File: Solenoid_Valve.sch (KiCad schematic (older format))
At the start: 62 parts, among them IC1 Si8621AB-B-ISR, J1 Bus_mechaken_PCIexpress_x16_1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, J10 Conn_01x02, J11 Conn_01x02, J12 Conn_01x02, J13 Conn_01x02, J14 Conn_01x02, J15 Conn_01x02, J16 Conn_01x02, J17 Conn_01x02, J18 Conn_01x02, J19 Conn_01x02, J2 Conn_01x05, J20 Conn_01x02, J3 Conn_01x02, J4 Conn_01x02, J5 Conn_01x02, J6 Conn_01x02, J7 Conn_01x03, J8 Conn_01x02, J9 Conn_01x02, Q1 ULN2004D1013TR, Q2 ULN2004D1013TR, Q3 ULN2004D1013TR, SW1 SW_Push, U1 LDL1117S33R, U2 STM32F042K6Tx, U3 MCP2562-E-SN, U4 L7812, U5 LDL1117S33R

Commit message: change
Remove NRST SW
clean
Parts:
- removed C3: 0.1uF, Capacitor_SMD:C_0805_2012Metric, symbol Device:C
- removed R3: 10K, Resistor_SMD:R_0603_1608Metric, symbol Device:R
- removed SW1: SW_Push, SamacSys_Parts:PTS647SM38SMTR2LFS, symbol Switch:SW_Push
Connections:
- wire segments 137 -> 131
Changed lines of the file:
@@
 EESchema Schematic File Version 4
-LIBS:Solenoid_Valve-cache
 EELAYER 30 0
 EELAYER END
@@
 Connection ~ 1350 1950
 Wire Wire Line
-	2800 1150 2800 1300
-Wire Wire Line
-	3700 1150 2800 1150
-Wire Wire Line
 	5450 3000 5450 3100
 Wire Wire Line
@@
 Wire Wire Line
 	900  1650 1000 1650
-Wire Wire Line
-	2300 2000 2800 2000
-Wire Wire Line
-	2300 1600 2800 1600
 Wire Wire Line
 	3700 1150 3950 1150
@@
 	3700 1050 3700 1150
 Connection ~ 3700 1150
-Connection ~ 2800 1600
 Wire Wire Line
 	3700 3300 3700 3400
@@
 Text GLabel 5750 3400 0    50   Input ~ 0
 NRST
-Text GLabel 3100 1600 1    50   Input ~ 0
+Text GLabel 3200 1600 0    50   Input ~ 0
 NRST
 Text GLabel 4200 3100 2    50   Input ~ 0
@@
 $EndComp
 $Comp
-L Switch:SW_Push SW1
-U 1 1 5D5B7C98
-P 2800 1800
-F 0 "SW1" V 2754 1752 50  0000 R CNN
-F 1 "SW_Push" V 2845 1752 50  0000 R CNN
-F 2 "SamacSys_Parts:PTS647SM38SMTR2LFS" H 2800 2000 50  0001 C CNN
-F 3 "~" H 2800 2000 50  0001 C CNN
-	1    2800 1800
-	0    -1   1    0
-$EndComp
-$Comp
-L Device:C C3
-U 1 1 5D5B9AC3
-P 2300 1750
-F 0 "C3" H 2415 1796 50  0000 L CNN
-F 1 "0.1uF" H 2415 1705 50  0000 L CNN
-F 2 "Capacitor_SMD:C_0805_2012Metric" H 2338 1600 50  0001 C CNN
-F 3 "~" H 2300 1750 50  0001 C CNN
-	1    2300 1750
-	1    0    0    -1
-$EndComp
-$Comp
-L Device:R R3
-U 1 1 5D5C9315
-P 2800 1450
-F 0 "R3" H 2870 1496 50  0000 L CNN
-F 1 "10K" H 2870 1405 50  0000 L CNN
-F 2 "Resistor_SMD:R_0603_1608Metric" V 2730 1450 50  0001 C CNN
-F 3 "~" H 2800 1450 50  0001 C CNN
-	1    2800 1450
-	1    0    0    -1
-$EndComp
-$Comp
 L Device:R R2
 U 1 1 5D5AB267
@@
 	0    1    1    0
 $EndComp
-Wire Wire Line
-	2300 1900 2300 2000
 Text Label 2850 3100 0    50   ~ 0
 BOOT
@@
 Wire Wire Line
 	6100 1350 6100 1450
-Text GLabel 5300 1150 0    50   Output ~ 0
+Text GLabel 5300 1350 0    50   Output ~ 0
 DIP_SW_1
-Text GLabel 5300 1250 0    50   Output ~ 0
+Text GLabel 5300 1450 0    50   Output ~ 0
 DIP_SW_2
-Wire Wire Line
-	3200 1600 2800 1600
 Connection ~ 3700 3300
 Wire Wire Line
@@
 	0    -1   -1   0
 $EndComp
-$Comp
-L power:GNDPWR #PWR05
-U 1 1 5DDA84FA
-P 2300 2000
-F 0 "#PWR05" H 2300 1800 50  0001 C CNN
-F 1 "GNDPWR" H 2300 1870 50  0000 C CNN
-F 2 "" H 2300 1950 50  0001 C CNN
-F 3 "" H 2300 1950 50  0001 C CNN
-	1    2300 2000
-	1    0    0    -1
-$EndComp
-Connection ~ 2300 2000
 $Comp
 L power:+3.3V #PWR01
@@
 Text GLabel 4200 2400 2    50   Input ~ 0
 IC_C3
-NoConn ~ 5300 1350
-NoConn ~ 5300 1450
 $Comp
 L power:GNDPWR #PWR0120
@@
 NoConn ~ 1150 7000
 $Comp
-L power:GNDPWR #PWR?
+L power:GNDPWR #PWR0115
 U 1 1 5DF51C19
 P 5250 1900
-F 0 "#PWR?" H 5250 1700 50  0001 C CNN
+F 0 "#PWR0115" H 5250 1700 50  0001 C CNN
 F 1 "GNDPWR" H 5250 1770 50  0000 C CNN
 F 2 "" H 5250 1850 50  0001 C CNN
@@
 	0    1    1    0
 $EndComp
+NoConn ~ 5300 1150
+NoConn ~ 5300 1250
 $EndSCHEMATC

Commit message: Prototype-1.1
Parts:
- Q1, Q2, Q3: symbol dk_Transistors-Bipolar-BJT-Arrays:ULN2003D1013TR -> Solenoid_Valve-rescue:ULN2003D1013TR-dk_Transistors-Bipolar-BJT-Arrays
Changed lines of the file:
@@
 DIP_SW_2
 $Comp
-L dk_Transistors-Bipolar-BJT-Arrays:ULN2003D1013TR Q1
+L Solenoid_Valve-rescue:ULN2003D1013TR-dk_Transistors-Bipolar-BJT-Arrays Q1
 U 1 1 5DC2DB55
 P 7500 2150
@@
 $EndComp
 $Comp
-L dk_Transistors-Bipolar-BJT-Arrays:ULN2003D1013TR Q2
+L Solenoid_Valve-rescue:ULN2003D1013TR-dk_Transistors-Bipolar-BJT-Arrays Q2
 U 1 1 5DC99CAB
 P 7500 3550
@@
 $EndComp
 $Comp
-L dk_Transistors-Bipolar-BJT-Arrays:ULN2003D1013TR Q3
+L Solenoid_Valve-rescue:ULN2003D1013TR-dk_Transistors-Bipolar-BJT-Arrays Q3
 U 1 1 5DCA1834
 P 7500 4950

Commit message: fix
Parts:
- C7: value 1uF -> 0.33uF
- C8: value 4.7uF -> 0.1uF
- J1: footprint PCIe:BUS_mechaken_PCIexpress_x16_164_Position -> PCIe:BUS_mechaken_PCIexpress_x16
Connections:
- net +3V3: no longer R2.2
- net GNDPWR: now also R2.2
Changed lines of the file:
@@
 	1    0    0    -1
-$EndComp
-$Comp
-L power:+3V3 #PWR08
-U 1 1 5DE307DF
-P 2500 3100
-F 0 "#PWR08" H 2500 2950 50  0001 C CNN
-F 1 "+3V3" H 2500 3240 50  0000 C CNN
-F 2 "" H 2500 3100 50  0001 C CNN
-F 3 "" H 2500 3100 50  0001 C CNN
-	1    2500 3100
-	-1   0    0    1
 $EndComp
 Text GLabel 3200 2500 0    50   Input ~ 0
@@
 P 7250 1150
 F 0 "C8" H 7275 1250 50  0000 L CNN
-F 1 "4.7uF" H 7275 1050 50  0000 L CNN
+F 1 "0.1uF" H 7275 1050 50  0000 L CNN
 F 2 "Capacitor_SMD:C_0805_2012Metric" H 7288 1000 50  0001 C CNN
 F 3 "~" H 7250 1150 50  0001 C CNN
@@
 P 6650 1150
 F 0 "C7" H 6675 1250 50  0000 L CNN
-F 1 "1uF" H 6675 1050 50  0000 L CNN
+F 1 "0.33uF" H 6675 1050 50  0000 L CNN
 F 2 "Capacitor_SMD:C_0805_2012Metric_Pad1.15x1.40mm_HandSolder" H 6688 1000 50  0001 C CNN
 F 3 "~" H 6650 1150 50  0001 C CNN
@@
 F 0 "J1" H 1700 12100 50  0000 C CNN
 F 1 "Bus_mechaken_PCIexpress_x16_164_Position" H 1650 10700 50  0000 C CNN
-F 2 "PCIe:BUS_mechaken_PCIexpress_x16_164_Position" H 1350 8900 50  0001 C CNN
+F 2 "PCIe:BUS_mechaken_PCIexpress_x16" H 1350 8900 50  0001 C CNN
 F 3 "http://pinouts.ru/Slots/PCI_pinout.shtml" H 1350 8900 50  0001 C CNN
 	1    1700 9000
@@
 NoConn ~ 5300 1150
 NoConn ~ 5300 1250
+$Comp
+L power:GNDPWR #PWR?
+U 1 1 5E334F41
+P 2500 3100
+F 0 "#PWR?" H 2500 2900 50  0001 C CNN
+F 1 "GNDPWR" H 2500 2970 50  0000 C CNN
+F 2 "" H 2500 3050 50  0001 C CNN
+F 3 "" H 2500 3050 50  0001 C CNN
+	1    2500 3100
+	1    0    0    -1
+$EndComp
 $EndSCHEMATC

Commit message: Release
Prototype-1.3をリリース
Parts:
- removed D1: LED, Diode_SMD:D_0603_1608Metric, symbol Device:LED
- removed R1: 10K, Resistor_SMD:R_0603_1608Metric, symbol Device:R
- added D11: D_Schottky, Diode_SMD:D_0603_1608Metric_Pad1.05x0.95mm_HandSolder, symbol Device:D_Schottky
- C1: renamed from C4; value 0.1uF -> 0.1u; footprint Capacitor_SMD:C_0805_2012Metric -> Capacitor_SMD:C_0805_2012Metric_Pad1.15x1.40mm_HandSolder
- C2: renamed from C7; value 0.33uF -> 0.33u
- C3: renamed from C8; value 0.1uF -> 0.1u; footprint Capacitor_SMD:C_0805_2012Metric -> Capacitor_SMD:C_0805_2012Metric_Pad1.15x1.40mm_HandSolder
- C4: renamed from C1; value 1.0uF -> 1.0u; footprint Capacitor_SMD:C_0805_2012Metric -> Capacitor_SMD:C_0805_2012Metric_Pad1.15x1.40mm_HandSolder
- C5: renamed from C2; value 4.7uF -> 2.2u; footprint Capacitor_SMD:C_0805_2012Metric -> Capacitor_SMD:C_0805_2012Metric_Pad1.15x1.40mm_HandSolder
- C6: value 0.1uF -> 0.1u; footprint Capacitor_SMD:C_0805_2012Metric -> Capacitor_SMD:C_0805_2012Metric_Pad1.15x1.40mm_HandSolder
- C7: renamed from C9; value 1.0uF -> 1.0u; footprint Capacitor_SMD:C_0805_2012Metric -> Capacitor_SMD:C_0805_2012Metric_Pad1.15x1.40mm_HandSolder
- C8: renamed from C10; value 4.7uF -> 4.7u; footprint Capacitor_SMD:C_0805_2012Metric -> Capacitor_SMD:C_0805_2012Metric_Pad1.15x1.40mm_HandSolder
- C9: renamed from C5; value 0.1uF -> 0.1u; footprint Capacitor_SMD:C_0805_2012Metric -> Capacitor_SMD:C_0805_2012Metric_Pad1.15x1.40mm_HandSolder
- D1: renamed from D6; footprint Diode_SMD:D_2010_5025Metric -> Diode_SMD:D_2010_5025Metric_Pad1.52x2.65mm_HandSolder
- D10: renamed from D17; footprint Diode_SMD:D_2010_5025Metric -> Diode_SMD:D_2010_5025Metric_Pad1.52x2.65mm_HandSolder
- D12: footprint Diode_SMD:D_2010_5025Metric -> Diode_SMD:D_2010_5025Metric_Pad1.52x2.65mm_HandSolder
- D13: renamed from D18; footprint Diode_SMD:D_2010_5025Metric -> Diode_SMD:D_2010_5025Metric_Pad1.52x2.65mm_HandSolder
- D14: renamed from D2; footprint Diode_SMD:D_2010_5025Metric -> Diode_SMD:D_2010_5025Metric_Pad1.52x2.65mm_HandSolder
- D15: renamed from D16; footprint Diode_SMD:D_2010_5025Metric -> Diode_SMD:D_2010_5025Metric_Pad1.52x2.65mm_HandSolder
- D16: renamed from D3; footprint Diode_SMD:D_2010_5025Metric -> Diode_SMD:D_2010_5025Metric_Pad1.52x2.65mm_HandSolder
- D17: renamed from D10; footprint Diode_SMD:D_2010_5025Metric -> Diode_SMD:D_2010_5025Metric_Pad1.52x2.65mm_HandSolder
- D18: renamed from D4; footprint Diode_SMD:D_2010_5025Metric -> Diode_SMD:D_2010_5025Metric_Pad1.52x2.65mm_HandSolder
- D2: renamed from D9; footprint Diode_SMD:D_2010_5025Metric -> Diode_SMD:D_2010_5025Metric_Pad1.52x2.65mm_HandSolder
- D3: renamed from D7; footprint Diode_SMD:D_2010_5025Metric -> Diode_SMD:D_2010_5025Metric_Pad1.52x2.65mm_HandSolder
- D4: renamed from D14; footprint Diode_SMD:D_2010_5025Metric -> Diode_SMD:D_2010_5025Metric_Pad1.52x2.65mm_HandSolder
- D5: renamed from D8; footprint Diode_SMD:D_2010_5025Metric -> Diode_SMD:D_2010_5025Metric_Pad1.52x2.65mm_HandSolder
- D6: renamed from D15; footprint Diode_SMD:D_2010_5025Metric -> Diode_SMD:D_2010_5025Metric_Pad1.52x2.65mm_HandSolder
- D7: renamed from D19; footprint Diode_SMD:D_2010_5025Metric -> Diode_SMD:D_2010_5025Metric_Pad1.52x2.65mm_HandSolder
- D8: renamed from D13; footprint Diode_SMD:D_2010_5025Metric -> Diode_SMD:D_2010_5025Metric_Pad1.52x2.65mm_HandSolder
- D9: renamed from D11; footprint Diode_SMD:D_2010_5025Metric -> Diode_SMD:D_2010_5025Metric_Pad1.52x2.65mm_HandSolder
- J10: renamed from J2; footprint Connector_JST:JST_XH_B5B-XH-A_1x05_P2.50mm_Vertical -> Connector_PinHeader_2.54mm:PinHeader_1x05_P2.54mm_Vertical
- J5: renamed from J7; footprint Connector_JST:JST_XH_B3B-XH-A_1x03_P2.50mm_Vertical -> Connector_PinHeader_2.54mm:PinHeader_1x03_P2.54mm_Vertical
- R1: renamed from R2; footprint Resistor_SMD:R_0603_1608Metric -> Resistor_SMD:R_0603_1608Metric_Pad1.05x0.95mm_HandSolder
- S1: footprint SamacSys_Parts:SOP254P980X370-8N -> Package_DIP:DIP-8_W7.62mm; symbol SamacSys_Parts:IKD0403101 -> Switch:SW_DIP_x04; Description 4 Way Surface Mount DIP Switch SPST, Raised Actuator Slide 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 -> (none); Height 3.7 -> (none); Manufacturer_Name Apem -> (none); Manufacturer_Part_Number IKD0403101 -> (none); RS Part Number 8772264 -> (none); RS Price/Stock http://uk.rs-online.com/web/p/products/8772264 -> (none)
- U1: renamed from U4; value L7812 -> NJM7812
- U2: renamed from U1; value LDL1117S33R -> AP2210N-3.3TRG1; footprint Package_TO_SOT_SMD:SOT-223-3_TabPin2 -> Package_TO_SOT_SMD:SOT-23_Handsoldering; symbol Solenoid_Valve-rescue:AP1117-33-Regulator_Linear -> Regulator_Linear:LD1117S33TR_SOT223
- U4: renamed from U5; value LDL1117S33R -> AP2210N-3.3TRG1; footprint Package_TO_SOT_SMD:SOT-223-3_TabPin2 -> Package_TO_SOT_SMD:SOT-23_Handsoldering; symbol Solenoid_Valve-rescue:AP1117-33-Regulator_Linear -> Regulator_Linear:LD1117S33TR_SOT223
- renumbered J8 to J1, J12 to J11, J18 to J12, J19 to J14, J4 to J15, J17 to J16, J5 to J17, J11 to J18, J6 to J19, J10 to J2, J1 to J20, J15 to J4, J9 to J6, J16 to J7, J20 to J8, J14 to J9, U2 to U3, U3 to U5
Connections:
- net 3.3V: now also S1.1, S1.2, D11.2 (A); no longer S1.5, S1.6, S1.7, S1.8
- net DIP_SW_1: now also S1.8, U3.28 (PB5); no longer S1.3, U3.29 (PB6)
- net DIP_SW_2: now also S1.7, U3.29 (PB6); no longer S1.4, U3.30 (PB7)
- net IC_A1: now also Q1.7 (IN_7), U3.30 (PB7); no longer Q1.1 (IN_1), U3.15 (PB1)
- net IC_A2: now also Q1.6 (IN_6), U3.2 (PF0); no longer Q1.2 (IN_2), U3.14 (PB0)
- net IC_A3: now also Q1.5 (IN_5), U3.3 (PF1); no longer Q1.3 (IN_3), U3.13 (PA7)
- net IC_A4: now also U3.6 (PA0); no longer U3.12 (PA6)
- net IC_A5: now also Q1.3 (IN_3), U3.7 (PA1); no longer Q1.5 (IN_5), U3.11 (PA5)
- net IC_A6: now also Q1.2 (IN_2), U3.9 (PA3); no longer Q1.6 (IN_6), U3.10 (PA4)
- net IC_B1: now also Q2.7 (IN_7), U3.10 (PA4); no longer Q2.1 (IN_1), U3.26 (PB3)
- net IC_B2: now also Q2.6 (IN_6), U3.11 (PA5); no longer Q2.2 (IN_2), U3.27 (PB4)
- net IC_B3: now also Q2.5 (IN_5), U3.12 (PA6); no longer Q2.3 (IN_3), U3.28 (PB5)
- net IC_B4: now also U3.13 (PA7); no longer U3.7 (PA1)
- net IC_B5: now also Q2.3 (IN_3), U3.14 (PB0); no longer Q2.5 (IN_5), U3.6 (PA0)
- net IC_B6: now also Q2.2 (IN_2), U3.15 (PB1); no longer Q2.6 (IN_6), U3.3 (PF1)
- net IC_C1: now also Q3.5 (IN_5); no longer Q3.1 (IN_1)
- net IC_C2: now also Q3.4 (IN_4); no longer Q3.2 (IN_2)
- net Solenoid_A1: now also D7.2 (A), J8.2 (Pin_2), Q1.10 (OUT_7); no longer D1.2 (A), J1.2 (Pin_2), Q1.16 (OUT_1)
- net Solenoid_A2: now also D13.2 (A), J14.2 (Pin_2), Q1.11 (OUT_6); no longer D3.2 (A), J3.2 (Pin_2), Q1.15 (OUT_2)
- net Solenoid_A3: now also D8.2 (A), J9.2 (Pin_2), Q1.12 (OUT_5); no longer D5.2 (A), J6.2 (Pin_2), Q1.14 (OUT_3)
- net Solenoid_A4: now also D10.2 (A), J12.2 (Pin_2); no longer D2.2 (A), J2.2 (Pin_2)
- net Solenoid_A5: now also D12.2 (A), J13.2 (Pin_2), Q1.14 (OUT_3); no longer D4.2 (A), J4.2 (Pin_2), Q1.12 (OUT_5)
- net Solenoid_A6: now also D9.2 (A), J11.2 (Pin_2), Q1.15 (OUT_2); no longer D6.2 (A), J7.2 (Pin_2), Q1.11 (OUT_6)
- net Solenoid_B1: now also D1.2 (A), J1.2 (Pin_2), Q2.10 (OUT_7); no longer D17.2 (A), J18.2 (Pin_2), Q2.16 (OUT_1)
- net Solenoid_B2: now also D3.2 (A), J3.2 (Pin_2), Q2.11 (OUT_6); no longer D9.2 (A), J11.2 (Pin_2), Q2.15 (OUT_2)
- net Solenoid_B3: now also D5.2 (A), J6.2 (Pin_2), Q2.12 (OUT_5); no longer D12.2 (A), J13.2 (Pin_2), Q2.14 (OUT_3)
- net Solenoid_B4: now also D2.2 (A), J2.2 (Pin_2); no longer D8.2 (A), J9.2 (Pin_2)
- net Solenoid_B5: now also D4.2 (A), J4.2 (Pin_2), Q2.14 (OUT_3); no longer D10.2 (A), J12.2 (Pin_2), Q2.12 (OUT_5)
- net Solenoid_B6: now also D6.2 (A), J7.2 (Pin_2), Q2.15 (OUT_2); no longer D13.2 (A), J14.2 (Pin_2), Q2.11 (OUT_6)
- net Solenoid_C1: now also D16.2 (A), J17.2 (Pin_2), Q3.12 (OUT_5); no longer D14.2 (A), J15.2 (Pin_2), Q3.16 (OUT_1)
- net Solenoid_C2: now also D18.2 (A), J19.2 (Pin_2), Q3.13 (OUT_4); no longer D16.2 (A), J17.2 (Pin_2), Q3.15 (OUT_2)
- net Solenoid_C3: now also D14.2 (A), J15.2 (Pin_2); no longer D18.2 (A), J19.2 (Pin_2)
- net VCC: now also D11.1 (K)
- removed net IC_A7: Q1.7 (IN_7), U3.9 (PA3)
- removed net IC_B7: Q2.7 (IN_7), U3.2 (PF0)
- net Solenoid_A7 renamed Solenoid_C4
- net Solenoid_C4: now also Q3.15 (OUT_2); no longer Q1.10 (OUT_7)
- removed net Solenoid_B7: D7.2 (A), J8.2 (Pin_2), Q2.10 (OUT_7)
- new net IC_C4: Q3.2 (IN_2), U3.26 (PB3)
- new net IC_C5: Q3.1 (IN_1), U3.27 (PB4)
- new net Solenoid_C5: D17.2 (A), J18.2 (Pin_2), Q3.16 (OUT_1)
- no-connect marks 19 -> 22
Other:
- moved on the sheet: C7, C8, D10, D12, D13, D14, D15, D16, D17, D18, D2, D4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

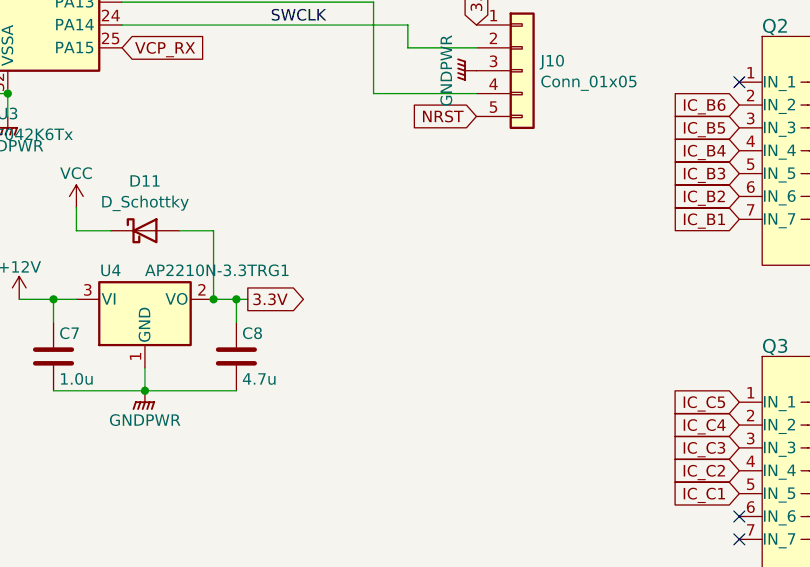
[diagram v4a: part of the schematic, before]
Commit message: Update: フットプリントライブラリの変更
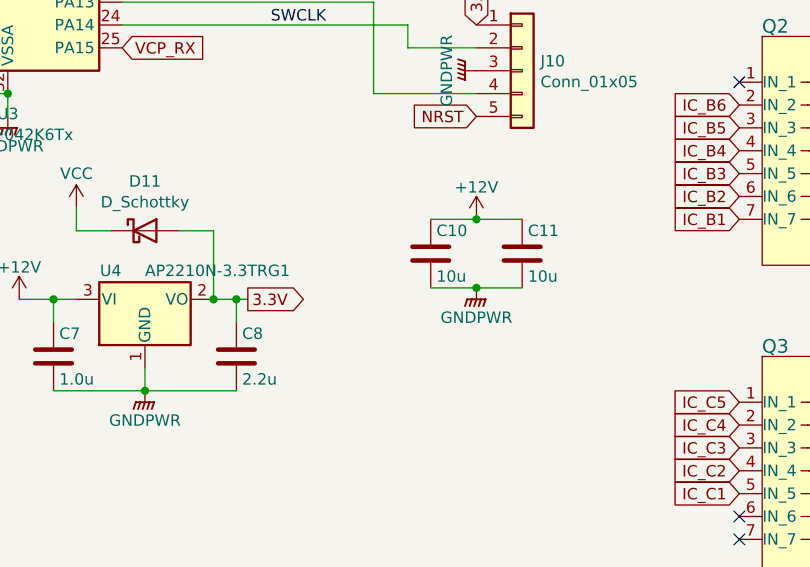
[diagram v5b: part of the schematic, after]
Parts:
- added C10, C11: 10u, Capacitor_SMD:C_0805_2012Metric_Pad1.18x1.45mm_HandSolder, symbol Device:C
- C1, C2, C3, C4, C5, C6, C7, C9: footprint Capacitor_SMD:C_0805_2012Metric_Pad1.15x1.40mm_HandSolder -> Capacitor_SMD:C_0805_2012Metric_Pad1.18x1.45mm_HandSolder
- C8: value 4.7u -> 2.2u; footprint Capacitor_SMD:C_0805_2012Metric_Pad1.15x1.40mm_HandSolder -> Capacitor_SMD:C_0805_2012Metric_Pad1.18x1.45mm_HandSolder
- R1: footprint Resistor_SMD:R_0603_1608Metric_Pad1.05x0.95mm_HandSolder -> Resistor_SMD:R_0603_1608Metric_Pad0.98x0.95mm_HandSolder
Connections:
- net +12V: now also C10.1, C11.1
- net GNDPWR: now also C10.2, C11.2
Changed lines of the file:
@@
 F 0 "C6" V 1998 3850 50  0000 C CNN
 F 1 "0.1u" V 2089 3850 50  0000 C CNN
-F 2 "Capacitor_SMD:C_0805_2012Metric_Pad1.15x1.40mm_HandSolder" H 2288 3700 50  0001 C CNN
+F 2 "Capacitor_SMD:C_0805_2012Metric_Pad1.18x1.45mm_HandSolder" H 2288 3700 50  0001 C CNN
 F 3 "~" H 2250 3850 50  0001 C CNN
 	1    2250 3850
@@
 F 0 "C9" V 598 4500 50  0000 C CNN
 F 1 "0.1u" V 689 4500 50  0000 C CNN
-F 2 "Capacitor_SMD:C_0805_2012Metric_Pad1.15x1.40mm_HandSolder" H 888 4350 50  0001 C CNN
+F 2 "Capacitor_SMD:C_0805_2012Metric_Pad1.18x1.45mm_HandSolder" H 888 4350 50  0001 C CNN
 F 3 "~" H 850 4500 50  0001 C CNN
 	1    850  4500
@@
 F 0 "C4" V 748 1800 50  0000 C CNN
 F 1 "1.0u" V 839 1800 50  0000 C CNN
-F 2 "Capacitor_SMD:C_0805_2012Metric_Pad1.15x1.40mm_HandSolder" H 1038 1650 50  0001 C CNN
+F 2 "Capacitor_SMD:C_0805_2012Metric_Pad1.18x1.45mm_HandSolder" H 1038 1650 50  0001 C CNN
 F 3 "~" H 1000 1800 50  0001 C CNN
 	1    1000 1800
@@
 F 0 "C5" V 1448 1800 50  0000 C CNN
 F 1 "2.2u" V 1539 1800 50  0000 C CNN
-F 2 "Capacitor_SMD:C_0805_2012Metric_Pad1.15x1.40mm_HandSolder" H 1738 1650 50  0001 C CNN
+F 2 "Capacitor_SMD:C_0805_2012Metric_Pad1.18x1.45mm_HandSolder" H 1738 1650 50  0001 C CNN
 F 3 "~" H 1700 1800 50  0001 C CNN
 	1    1700 1800
@@
 F 0 "C1" V 3848 1150 50  0000 C CNN
 F 1 "0.1u" V 3939 1150 50  0000 C CNN
-F 2 "Capacitor_SMD:C_0805_2012Metric_Pad1.15x1.40mm_HandSolder" H 4138 1000 50  0001 C CNN
+F 2 "Capacitor_SMD:C_0805_2012Metric_Pad1.18x1.45mm_HandSolder" H 4138 1000 50  0001 C CNN
 F 3 "~" H 4100 1150 50  0001 C CNN
 	1    4100 1150
@@
 F 0 "R1" V 2443 3100 50  0000 C CNN
 F 1 "10K" V 2534 3100 50  0000 C CNN
-F 2 "Resistor_SMD:R_0603_1608Metric_Pad1.05x0.95mm_HandSolder" V 2580 3100 50  0001 C CNN
+F 2 "Resistor_SMD:R_0603_1608Metric_Pad0.98x0.95mm_HandSolder" V 2580 3100 50  0001 C CNN
 F 3 "~" H 2650 3100 50  0001 C CNN
 	1    2650 3100
@@
 Text GLabel 3200 3000 0    50   Input ~ 0
 IC_A1
-$Comp
-L Solenoid_Valve-rescue:ULN2003D1013TR-dk_Transistors-Bipolar-BJT-Arrays Q1
-U 1 1 5DC2DB55
-P 7500 2150
-F 0 "Q1" H 6999 2694 60  0000 L CNN
-F 1 "ULN2004D1013TR" H 7507 1600 60  0000 L CNN
-F 2 "digikey-footprints:SOIC-16_W3.90mm" H 7700 2350 60  0001 L CNN
-F 3 "http://www.st.com/content/ccc/resource/technical/document/datasheet/f3/6e/c8/64/4d/b3/4e/38/CD00001244.pdf/files/CD00001244.pdf/jcr:content/translations/en.CD00001244.pdf" H 7700 2450 60  0001 L CNN
-F 4 "497-2345-1-ND" H 7700 2550 60  0001 L CNN "Digi-Key_PN"
-F 5 "ULN2003D1013TR" H 7700 2650 60  0001 L CNN "MPN"
-F 6 "Discrete Semiconductor Products" H 7700 2750 60  0001 L CNN "Category"
-F 7 "Transistors - Bipolar (BJT) - Arrays" H 7700 2850 60  0001 L CNN "Family"
-F 8 "http://www.st.com/content/ccc/resource/technical/document/datasheet/f3/6e/c8/64/4d/b3/4e/38/CD00001244.pdf/files/CD00001244.pdf/jcr:content/translations/en.CD00001244.pdf" H 7700 2950 60  0001 L CNN "DK_Datasheet_Link"
-F 9 "/product-detail/en/stmicroelectronics/ULN2003D1013TR/497-2345-1-ND/599201" H 7700 3050 60  0001 L CNN "DK_Detail_Page"
-F 10 "IC PWR RELAY 7NPN 1:1 16SO" H 7700 3150 60  0001 L CNN "Description"
-F 11 "STMicroelectronics" H 7700 3250 60  0001 L CNN "Manufacturer"
-F 12 "Active" H 7700 3350 60  0001 L CNN "Status"
-	1    7500 2150
-	1    0    0    -1
-$EndComp
 Text GLabel 8100 1950 2    50   UnSpc ~ 0
 Solenoid_A6
@@
 Text GLabel 9250 1650 0    50   UnSpc ~ 0
 Solenoid_B2
-Text GLabel 6900 2450 0    50   Input ~ 0
-IC_A1
-Text GLabel 6900 2350 0    50   Input ~ 0
-IC_A2
-Text GLabel 6900 2250 0    50   Input ~ 0
-IC_A3
-Text GLabel 6900 2150 0    50   Input ~ 0
-IC_A4
-Text GLabel 6900 2050 0    50   Input ~ 0
-IC_A5
-Text GLabel 6900 1950 0    50   Input ~ 0
-IC_A6
 $Comp
 L power:GNDPWR #PWR038
@@
 F 0 "C3" H 7275 1250 50  0000 L CNN
 F 1 "0.1u" H 7275 1050 50  0000 L CNN
-F 2 "Capacitor_SMD:C_0805_2012Metric_Pad1.15x1.40mm_HandSolder" H 7288 1000 50  0001 C CNN
+F 2 "Capacitor_SMD:C_0805_2012Metric_Pad1.18x1.45mm_HandSolder" H 7288 1000 50  0001 C CNN
 F 3 "~" H 7250 1150 50  0001 C CNN
 	1    7250 1150
@@
 F 0 "C2" H 6675 1250 50  0000 L CNN
 F 1 "0.33u" H 6675 1050 50  0000 L CNN
-F 2 "Capacitor_SMD:C_0805_2012Metric_Pad1.15x1.40mm_HandSolder" H 6688 1000 50  0001 C CNN
+F 2 "Capacitor_SMD:C_0805_2012Metric_Pad1.18x1.45mm_HandSolder" H 6688 1000 50  0001 C CNN
 F 3 "~" H 6650 1150 50  0001 C CNN
 	1    6650 1150
@@
 P 4700 4450
 F 0 "C8" H 4725 4550 50  0000 L CNN
-F 1 "4.7u" H 4725 4350 50  0000 L CNN
-F 2 "Capacitor_SMD:C_0805_2012Metric_Pad1.15x1.40mm_HandSolder" H 4738 4300 50  0001 C CNN
+F 1 "2.2u" H 4725 4350 50  0000 L CNN
+F 2 "Capacitor_SMD:C_0805_2012Metric_Pad1.18x1.45mm_HandSolder" H 4738 4300 50  0001 C CNN
 F 3 "~" H 4700 4450 50  0001 C CNN
 	1    4700 4450
@@
 F 0 "C7" H 3925 4550 50  0000 L CNN
 F 1 "1.0u" H 3925 4350 50  0000 L CNN
-F 2 "Capacitor_SMD:C_0805_2012Metric_Pad1.15x1.40mm_HandSolder" H 3938 4300 50  0001 C CNN
+F 2 "Capacitor_SMD:C_0805_2012Metric_Pad1.18x1.45mm_HandSolder" H 3938 4300 50  0001 C CNN
 F 3 "~" H 3900 4450 50  0001 C CNN
 	1    3900 4450
@@
 Wire Wire Line
 	5300 1350 5300 1450
+Text GLabel 6900 1950 0    50   Input ~ 0
+IC_A6
+Text GLabel 6900 2050 0    50   Input ~ 0
+IC_A5
+Text GLabel 6900 2150 0    50   Input ~ 0
+IC_A4
+Text GLabel 6900 2250 0    50   Input ~ 0
+IC_A3
+Text GLabel 6900 2350 0    50   Input ~ 0
+IC_A2
+Text GLabel 6900 2450 0    50   Input ~ 0
+IC_A1
+$Comp
+L Solenoid_Valve-rescue:ULN2003D1013TR-dk_Transistors-Bipolar-BJT-Arrays Q1
+U 1 1 5DC2DB55
+P 7500 2150
+F 0 "Q1" H 6999 2694 60  0000 L CNN
+F 1 "ULN2004D1013TR" H 7507 1600 60  0000 L CNN
+F 2 "digikey-footprints:SOIC-16_W3.90mm" H 7700 2350 60  0001 L CNN
+F 3 "http://www.st.com/content/ccc/resource/technical/document/datasheet/f3/6e/c8/64/4d/b3/4e/38/CD00001244.pdf/files/CD00001244.pdf/jcr:content/translations/en.CD00001244.pdf" H 7700 2450 60  0001 L CNN
+F 4 "497-2345-1-ND" H 7700 2550 60  0001 L CNN "Digi-Key_PN"
+F 5 "ULN2003D1013TR" H 7700 2650 60  0001 L CNN "MPN"
+F 6 "Discrete Semiconductor Products" H 7700 2750 60  0001 L CNN "Category"
+F 7 "Transistors - Bipolar (BJT) - Arrays" H 7700 2850 60  0001 L CNN "Family"
+F 8 "http://www.st.com/content/ccc/resource/technical/document/datasheet/f3/6e/c8/64/4d/b3/4e/38/CD00001244.pdf/files/CD00001244.pdf/jcr:content/translations/en.CD00001244.pdf" H 7700 2950 60  0001 L CNN "DK_Datasheet_Link"
+F 9 "/product-detail/en/stmicroelectronics/ULN2003D1013TR/497-2345-1-ND/599201" H 7700 3050 60  0001 L CNN "DK_Detail_Page"
+F 10 "IC PWR RELAY 7NPN 1:1 16SO" H 7700 3150 60  0001 L CNN "Description"
+F 11 "STMicroelectronics" H 7700 3250 60  0001 L CNN "Manufacturer"
+F 12 "Active" H 7700 3350 60  0001 L CNN "Status"
+	1    7500 2150
+	1    0    0    -1
+$EndComp
+$Comp
+L Device:C C10
+U 1 1 5FA2B975
+P 5550 4000
+F 0 "C10" H 5575 4100 50  0000 L CNN
+F 1 "10u" H 5575 3900 50  0000 L CNN
+F 2 "Capacitor_SMD:C_0805_2012Metric_Pad1.18x1.45mm_HandSolder" H 5588 3850 50  0001 C CNN
+F 3 "~" H 5550 4000 50  0001 C CNN
+	1    5550 4000
+	1    0    0    -1
+$EndComp
+$Comp
+L Device:C C11
+U 1 1 5FA309ED
+P 5950 4000
+F 0 "C11" H 5975 4100 50  0000 L CNN
+F 1 "10u" H 5975 3900 50  0000 L CNN
+F 2 "Capacitor_SMD:C_0805_2012Metric_Pad1.18x1.45mm_HandSolder" H 5988 3850 50  0001 C CNN
+F 3 "~" H 5950 4000 50  0001 C CNN
+	1    5950 4000
+	1    0    0    -1
+$EndComp
+$Comp
+L power:GNDPWR #PWR058
+U 1 1 5FA369E5
+P 5750 4150
+F 0 "#PWR058" H 5750 3950 50  0001 C CNN
+F 1 "GNDPWR" H 5750 4020 50  0000 C CNN
+F 2 "" H 5750 4100 50  0001 C CNN
+F 3 "" H 5750 4100 50  0001 C CNN
+	1    5750 4150
+	1    0    0    -1
+$EndComp
+$Comp
+L power:+12V #PWR057
+U 1 1 5FA42039
+P 5750 3850
+F 0 "#PWR057" H 5750 3700 50  0001 C CNN
+F 1 "+12V" H 5750 3990 50  0000 C CNN
+F 2 "" H 5750 3850 50  0001 C CNN
+F 3 "" H 5750 3850 50  0001 C CNN
+	1    5750 3850
+	1    0    0    -1
+$EndComp
+Wire Wire Line
+	5550 3850 5750 3850
+Connection ~ 5750 3850
+Wire Wire Line
+	5750 3850 5950 3850
+Wire Wire Line
+	5550 4150 5750 4150
+Connection ~ 5750 4150
+Wire Wire Line
+	5750 4150 5950 4150
 $EndSCHEMATC
